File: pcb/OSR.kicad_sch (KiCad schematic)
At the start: 86 parts, among them J1 Conn_01x10_Socket, J10 Conn_01x02_Socket, J11 Conn_01x02_Socket, J12 Conn_01x08_Socket, J13 Conn_01x04_Pin, J15 Conn_01x08_Socket, J2 Conn_01x02_Pin, J3 Conn_01x10_Socket, J4 Conn_02x02_Counter_Clockwise, J5 Conn_02x02_Counter_Clockwise, J6 Conn_02x02_Counter_Clockwise, J7 Conn_02x02_Counter_Clockwise, J8 Conn_02x02_Counter_Clockwise, J9 Conn_02x02_Counter_Clockwise, Q1 BUK7880-55A, Q10 AO3400A, Q11 AO3400A, Q12 AO3400A, Q13 AO3400A, Q14 AO3400A, Q15 AO3400A, Q16 AO3400A, Q17 AO3400A, Q2 MMBFJ113, Q3 MMBFJ113, Q4 MMBFJ113, Q5 MMBFJ113, Q6 MMBFJ113, Q7 MMBFJ113, Q8 MMBFJ113, Q9 MMBFJ113, SW1 SW_SPST, SW2 SW_SPST, U1 4011, U2 40106, U3 HEF4094B

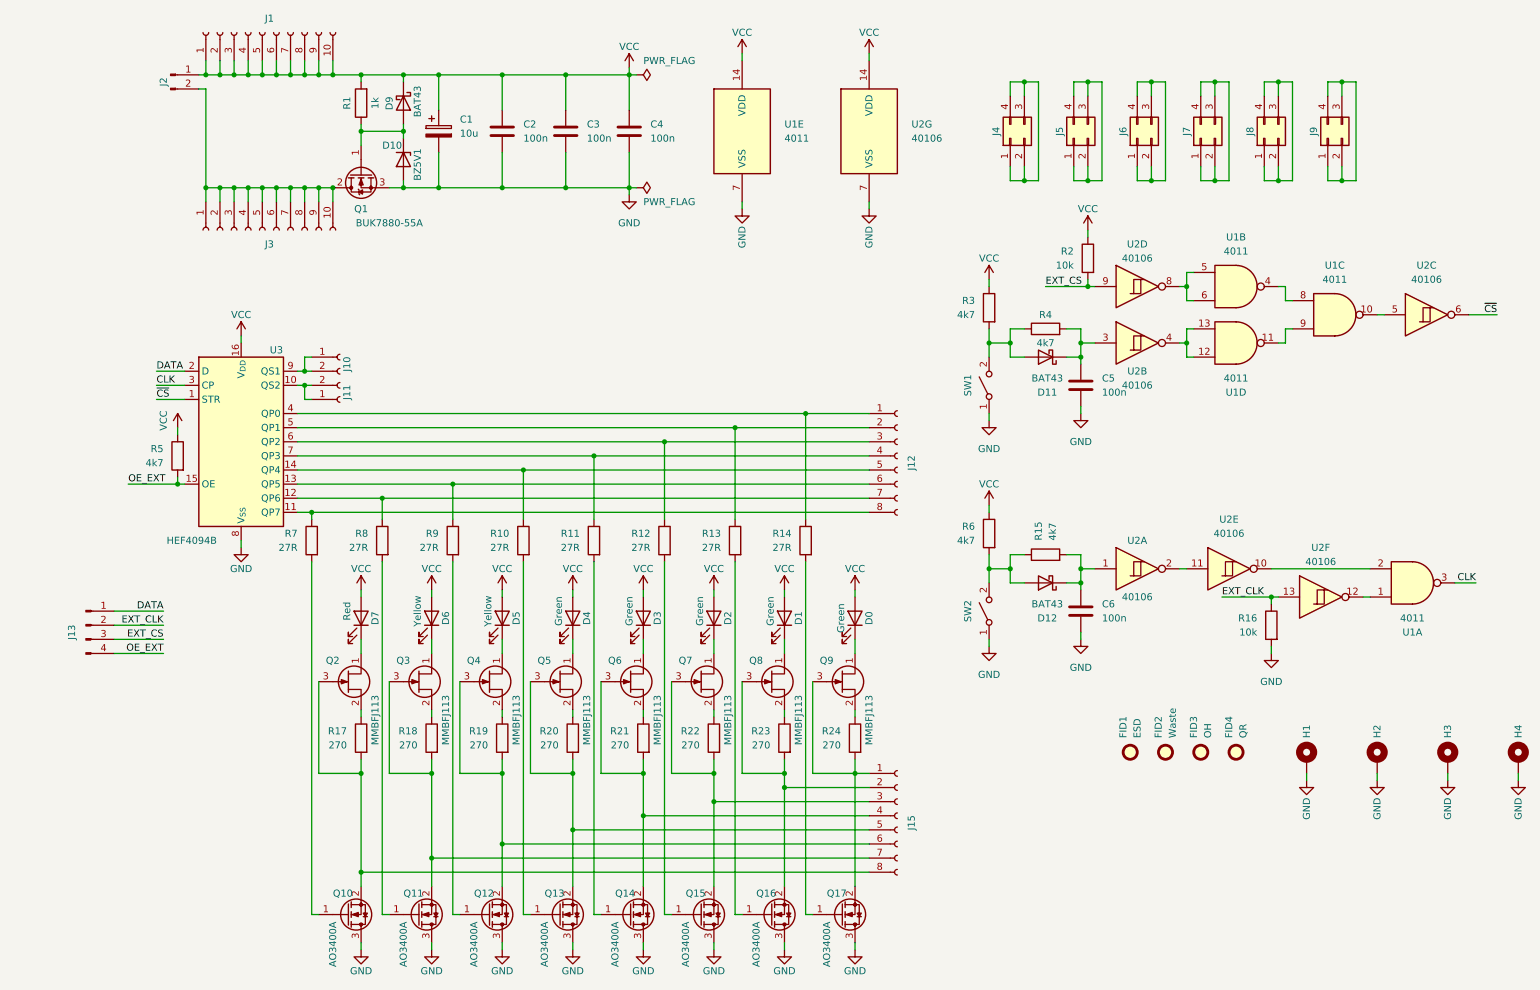
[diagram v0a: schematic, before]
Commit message: Add CLK and CS led beside push-button
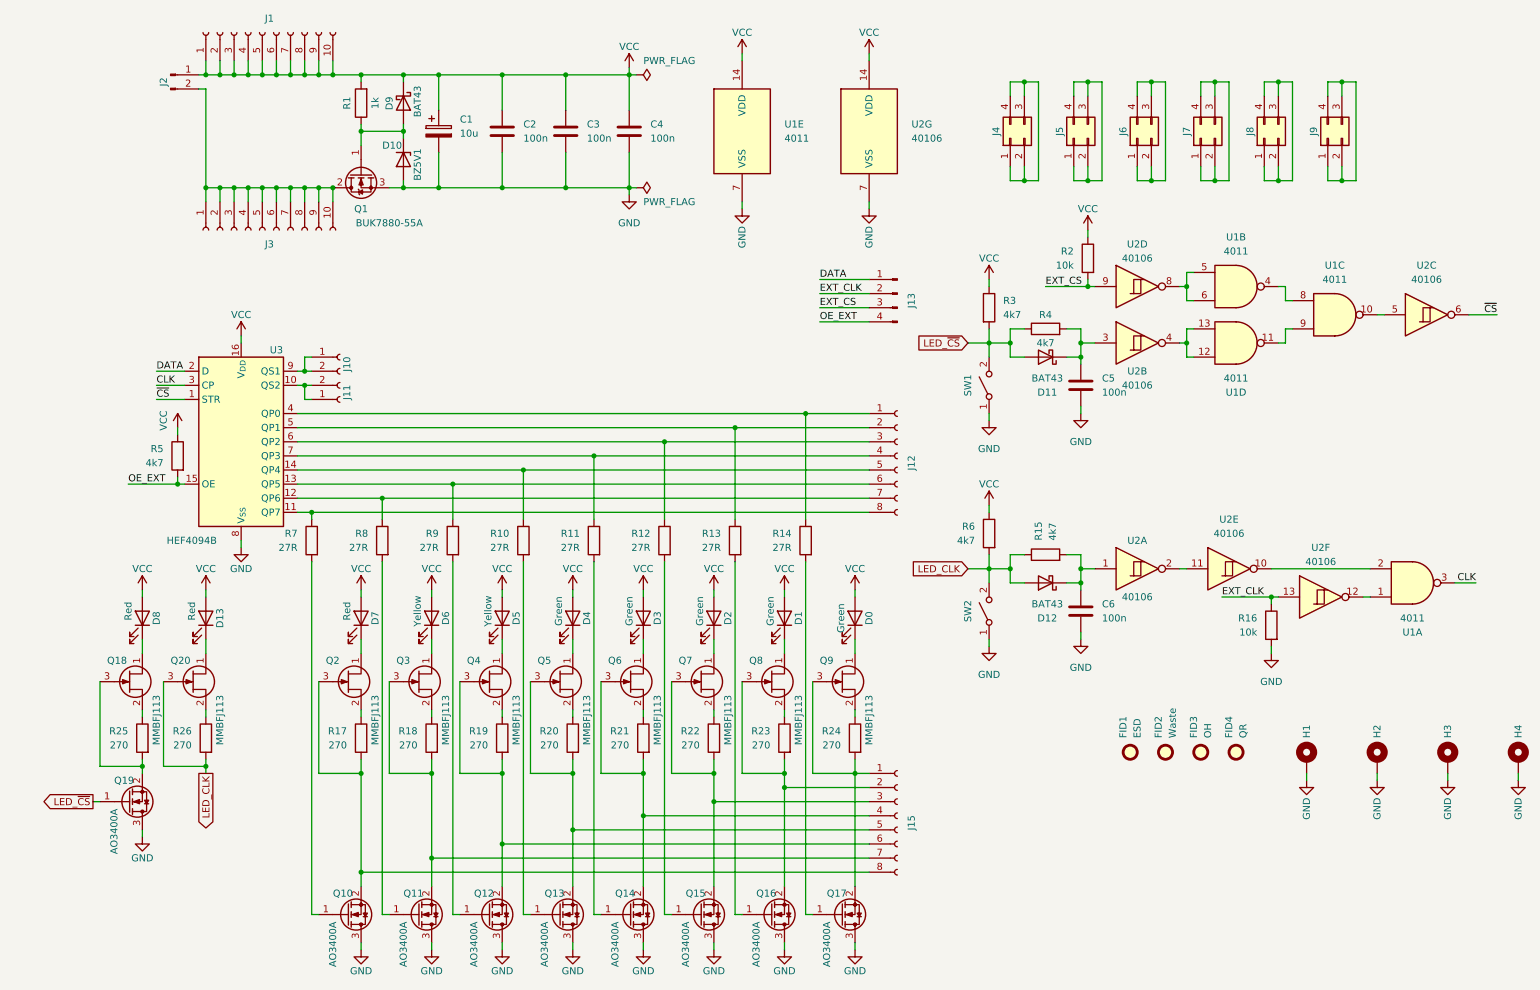
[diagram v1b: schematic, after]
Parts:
- added D13, D8: Red, LED_SMD:LED_1206_3216Metric, symbol Device:LED
- added Q18, Q20: MMBFJ113, Package_TO_SOT_SMD:SOT-23, symbol Transistor_FET:MMBFJ113
- added Q19: AO3400A, Package_TO_SOT_SMD:SOT-23-3, symbol Transistor_FET:AO3400A
- added R25, R26: 270, Resistor_SMD:R_1206_3216Metric, symbol Device:R
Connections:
- net GND: now also Q19.3 (D)
- net VCC: now also D13.2 (A), D8.2 (A)
- net LED_~{CS}: now reaches D11.2 (A), R3.2, R4.1, SW1.2 (B)
- net LED_~{CS}: now also Q19.1 (G)
- net LED_CLK: now reaches D12.2 (A), R15.1, R6.2, SW2.2 (B)
- net LED_CLK: now also Q20.3 (G), R26.2
- new net: Q18.2 (S), R25.1
- new net: Q18.3 (G), Q19.2 (S), R25.2
- new net: D13.1 (K), Q20.1 (D)
- new net: D8.1 (K), Q18.1 (D)
- new net: Q20.2 (S), R26.1
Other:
- moved on the sheet: J13
